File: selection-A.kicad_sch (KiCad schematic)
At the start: 4 parts, among them U0 74LS08, U10 74LS08, U12 74LS08, U13 74AHC1G32

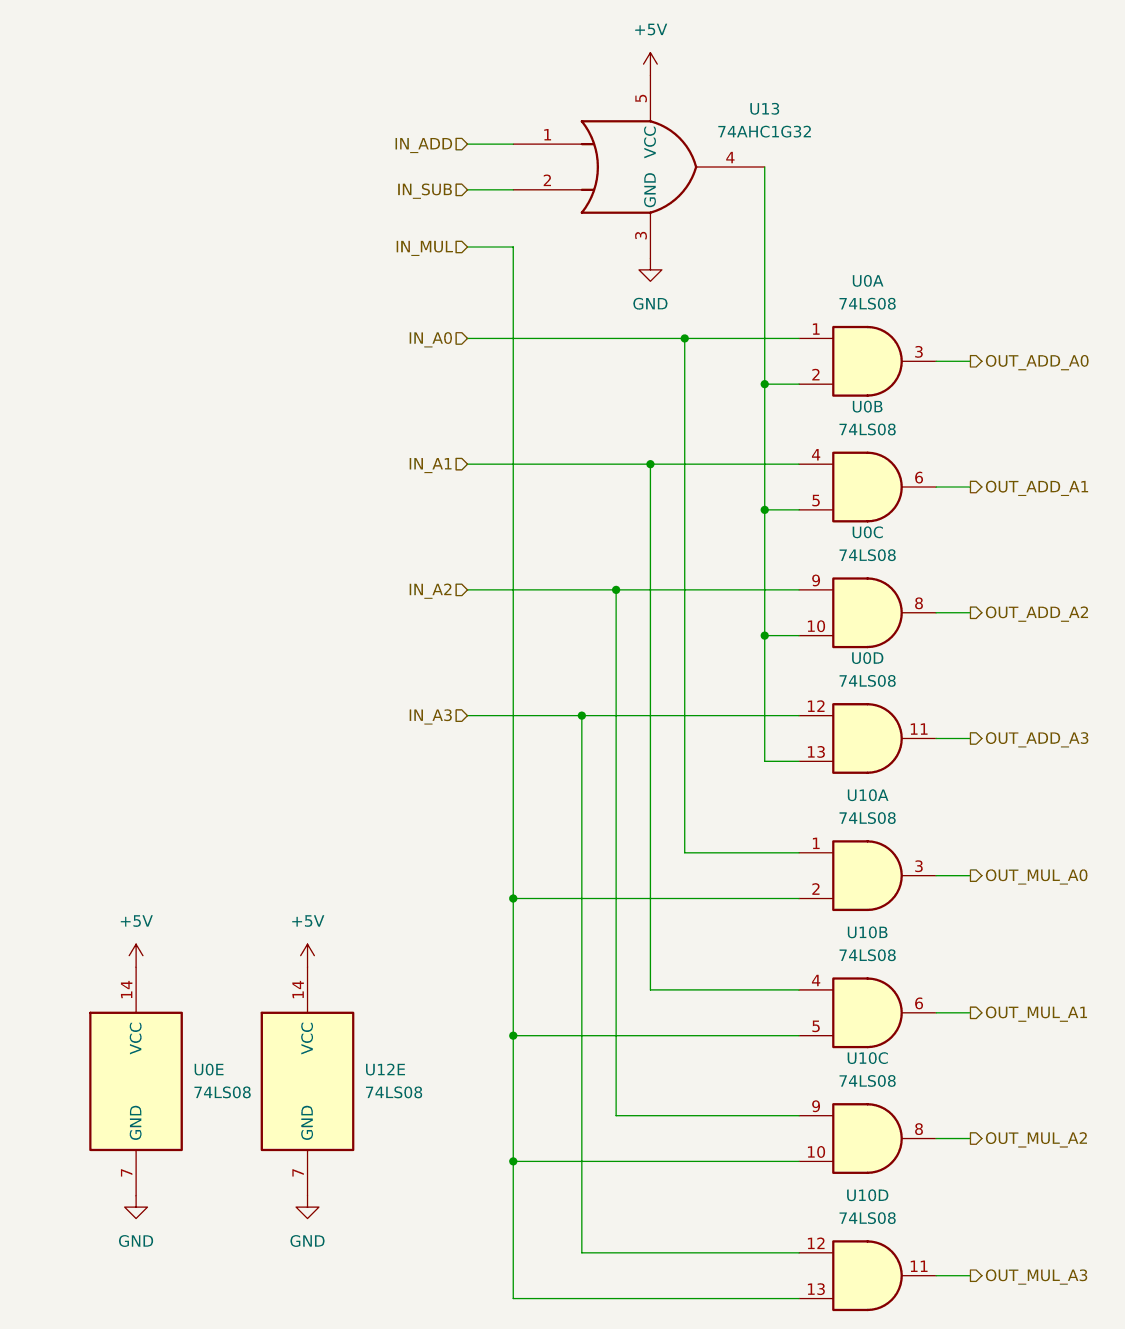
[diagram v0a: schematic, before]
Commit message: feat: removed ERC errors
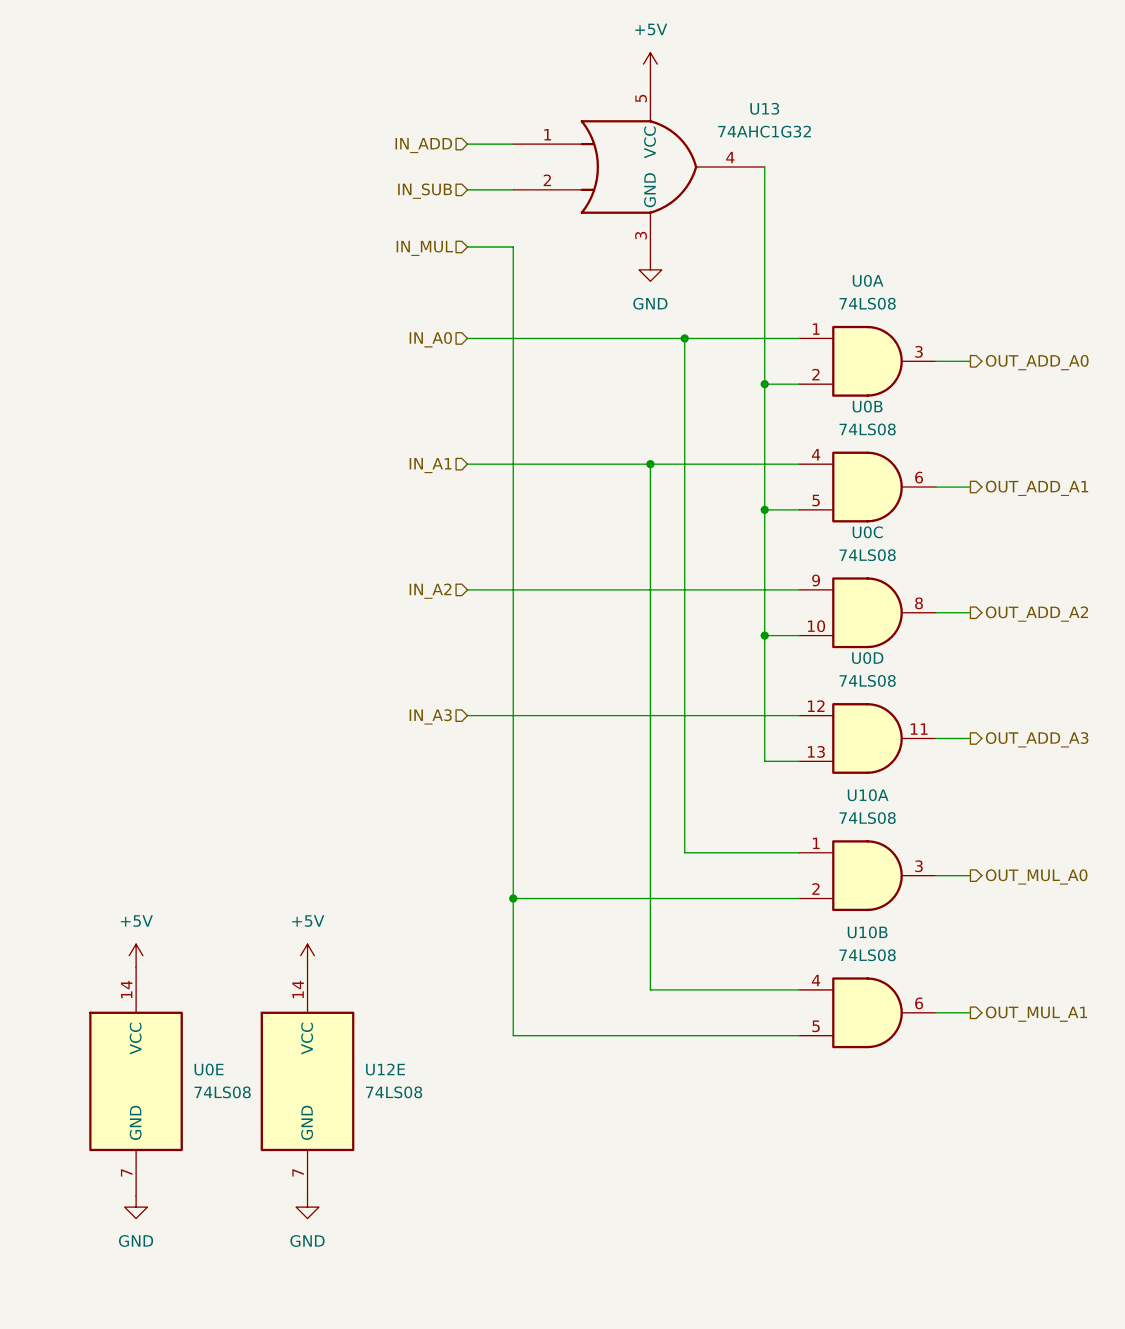
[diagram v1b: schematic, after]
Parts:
- removed unit 4 of U10
- removed unit 3 of U10

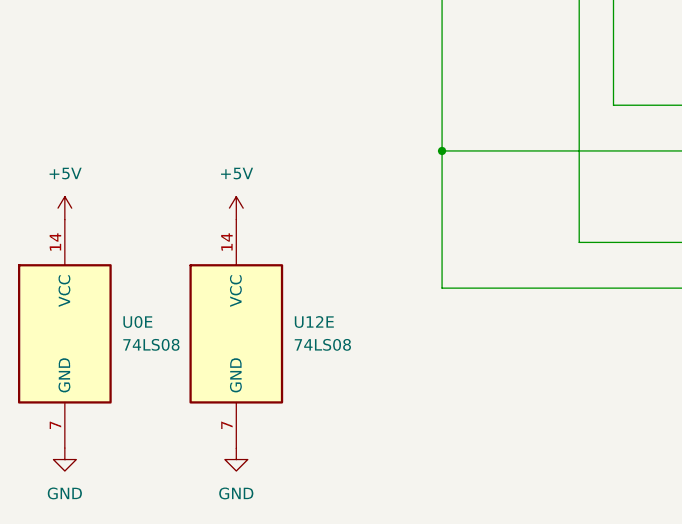
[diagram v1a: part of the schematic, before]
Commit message: fix: removed ERC warnings and errors
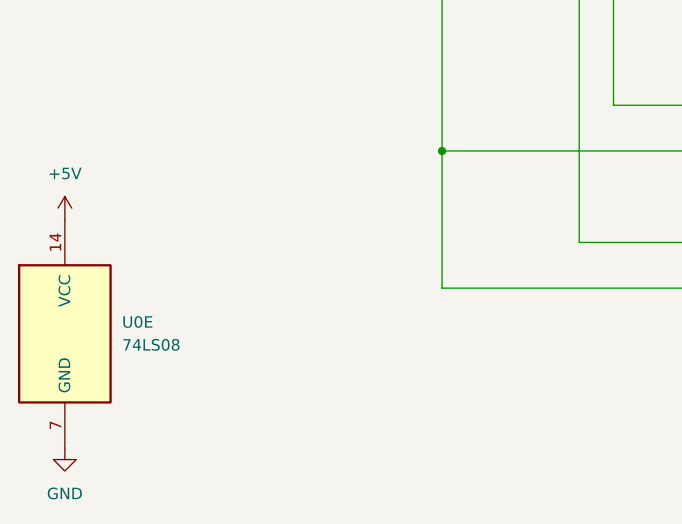
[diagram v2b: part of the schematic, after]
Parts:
- removed U12: 74LS08, symbol 74xx:74LS08
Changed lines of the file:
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@@
-	)
-	(symbol
-		(lib_id "power:GND")
-		(at 73.66 154.94 0)
-		(unit 1)
-		(exclude_from_sim no)
-		(in_bom yes)
-		(on_board yes)
-		(dnp no)
-		(fields_autoplaced yes)
-		(property "Reference" "#PWR025"
-			(at 73.66 161.29 0)
-			(effects
-				(font
-					(size 1.27 1.27)
-				)
-				(hide yes)
-			)
-		)
-		(property "Value" "GND"
-			(at 73.66 160.02 0)
-			(effects
-				(font
-					(size 1.27 1.27)
-				)
-			)
-		)
-		(property "Footprint" ""
-			(at 73.66 154.94 0)
-			(effects
-				(font
-					(size 1.27 1.27)
-				)
-				(hide yes)
-			)
-		)
-		(property "Datasheet" ""
-			(at 73.66 154.94 0)
-			(effects
-				(font
-					(size 1.27 1.27)
-				)
-				(hide yes)
-			)
-		)
-		(property "Description" "Power symbol creates a global label with name \"GND\" , ground"
-			(at 73.66 154.94 0)
-			(effects
-				(font
-					(size 1.27 1.27)
-				)
-				(hide yes)
-			)
-		)
-		(pin "1"
-		)
-		(instances
-			(project ""
-				(path "/4987240f-8890-46b8-b8e9-0d60580cb205/30c1ae8d-c878-40aa-ace0-371f489a4d3c"
-					(reference "#PWR025")
-					(unit 1)
-				)
-			)
-		)
 	)
 	(symbol
@@
 	(symbol
 		(lib_id "power:+5V")
-		(at 73.66 129.54 0)
-		(unit 1)
-		(exclude_from_sim no)
-		(in_bom yes)
-		(on_board yes)
-		(dnp no)
-		(fields_autoplaced yes)
-		(property "Reference" "#PWR06"
-			(at 73.66 133.35 0)
-			(effects
-				(font
-					(size 1.27 1.27)
-				)
-				(hide yes)
-			)
-		)
-		(property "Value" "+5V"
-			(at 73.66 124.46 0)
-			(effects
-				(font
-					(size 1.27 1.27)
-				)
-			)
-		)
-		(property "Footprint" ""
-			(at 73.66 129.54 0)
-			(effects
-				(font
-					(size 1.27 1.27)
-				)
-				(hide yes)
-			)
-		)
-		(property "Datasheet" ""
-			(at 73.66 129.54 0)
-			(effects
-				(font
-					(size 1.27 1.27)
-				)
-				(hide yes)
-			)
-		)
-		(property "Description" "Power symbol creates a global label with name \"+5V\""
-			(at 73.66 129.54 0)
-			(effects
-				(font
-					(size 1.27 1.27)
-				)
-				(hide yes)
-			)
-		)
-		(pin "1"
-		)
-		(instances
-			(project ""
-				(path "/4987240f-8890-46b8-b8e9-0d60580cb205/30c1ae8d-c878-40aa-ace0-371f489a4d3c"
-					(reference "#PWR06")
-					(unit 1)
-				)
-			)
-		)
-	)
-	(symbol
-		(lib_id "power:+5V")
 		(at 111.76 30.48 0)
 		(unit 1)
@@
 				)
 			)
-		)
-	)
-	(symbol
-		(lib_id "74xx:74LS08")
-		(at 73.66 142.24 0)
-		(unit 5)
-		(exclude_from_sim no)
-		(in_bom yes)
-		(on_board yes)
-		(dnp no)
-		(fields_autoplaced yes)
-		(property "Reference" "U12"
-			(at 80.01 140.9699 0)
-			(effects
-				(font
-					(size 1.27 1.27)
-				)
-				(justify left)
-			)
-		)
-		(property "Value" "74LS08"
-			(at 80.01 143.5099 0)
-			(effects
-				(font
-					(size 1.27 1.27)
-				)
-				(justify left)
-			)
-		)
-		(property "Footprint" ""
-			(at 73.66 142.24 0)
-			(effects
-				(font
-					(size 1.27 1.27)
-				)
-				(hide yes)
-			)
-		)
-		(property "Datasheet" "http://www.ti.com/lit/gpn/sn74LS08"
-			(at 73.66 142.24 0)
-			(effects
-				(font
-					(size 1.27 1.27)
-				)
-				(hide yes)
-			)
-		)
-		(property "Description" "Quad And2"
-			(at 73.66 142.24 0)
-			(effects
-				(font
-					(size 1.27 1.27)
-				)
-				(hide yes)
-			)
-		)
-		(pin "12"
-		)
-		(pin "14"
-		)
-		(pin "11"
-		)
-		(pin "7"
-		)
-		(pin "8"
-		)
-		(pin "10"
-		)
-		(pin "9"
-		)
-		(pin "6"
-		)
-		(pin "5"
-		)
-		(pin "4"
-		)
-		(pin "3"
-		)
-		(pin "2"
-		)
-		(pin "1"
-		)
-		(pin "13"
-		)
-		(instances
-			(project ""
-				(path "/4987240f-8890-46b8-b8e9-0d60580cb205/30c1ae8d-c878-40aa-ace0-371f489a4d3c"
-					(reference "U12")
-					(unit 5)
-				)
-			)

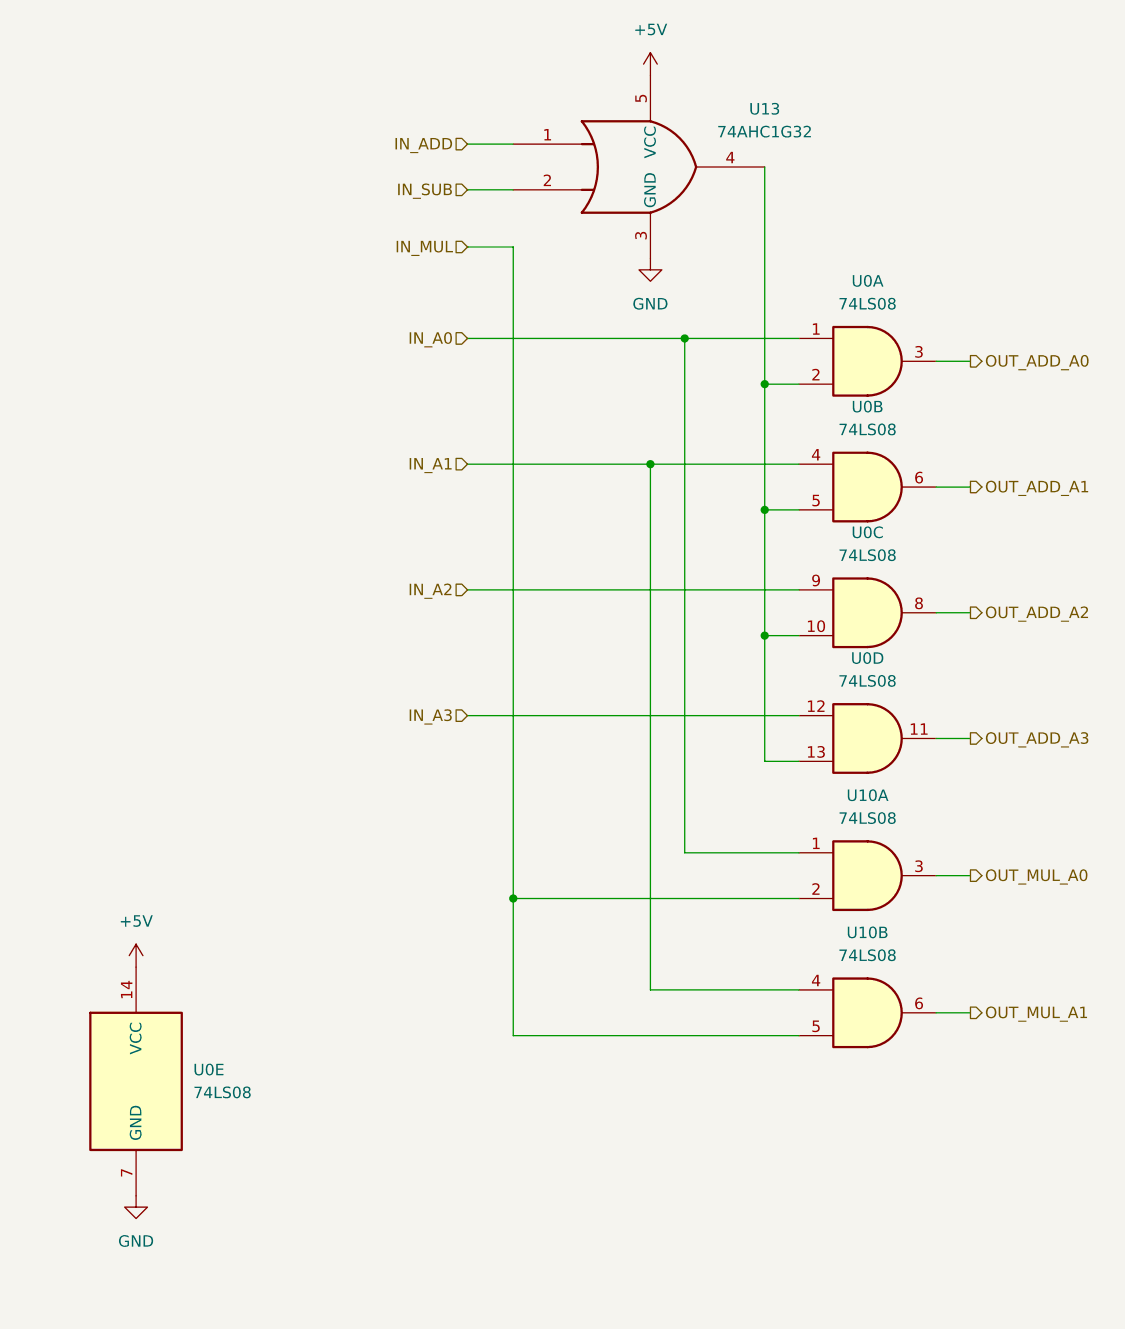
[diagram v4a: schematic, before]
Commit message: feat: footprints on gates
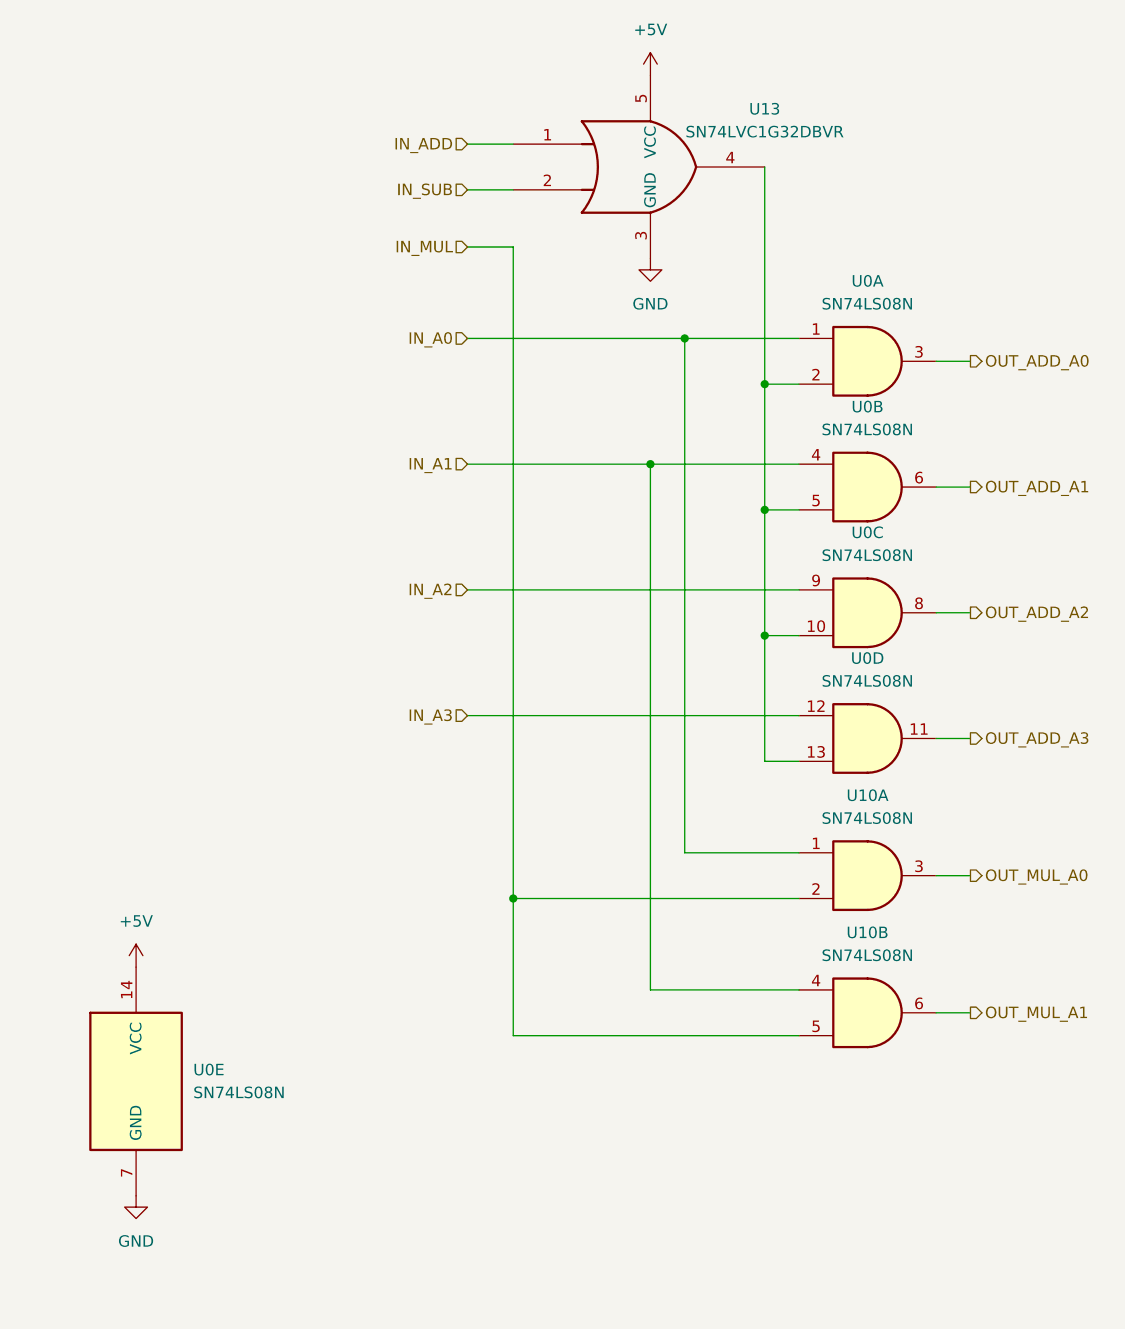
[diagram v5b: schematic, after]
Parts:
- U0, U10: value 74LS08 -> SN74LS08N; footprint (none) -> Package_DIP:DIP-14_W7.62mm_LongPads
- U13: value 74AHC1G32 -> SN74LVC1G32DBVR; footprint (none) -> Package_TO_SOT_SMD:SOT-23-5_HandSoldering
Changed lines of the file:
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@@
 			)
 		)
-		(property "Value" "74AHC1G32"
+		(property "Value" "SN74LVC1G32DBVR"
 			(at 124.46 36.7598 0)
 			(show_name no)
@@
 			)
 		)
-		(property "Footprint" ""
+		(property "Footprint" "Package_TO_SOT_SMD:SOT-23-5_HandSoldering"
 			(at 111.76 40.64 0)
 			(hide yes)
@@
 			)
 		)
-		(property "Value" "74LS08"
+		(property "Value" "SN74LS08N"
 			(at 135.8817 69.85 0)
 			(show_name no)
@@
 			)
 		)
-		(property "Footprint" ""
+		(property "Footprint" "Package_DIP:DIP-14_W7.62mm_LongPads"
 			(at 135.89 76.2 0)
 			(hide yes)
@@
 			)
 		)
-		(property "Datasheet" "http://www.ti.com/lit/gpn/sn74LS08"
+		(property "Datasheet" "https://www.ti.com/lit/ds/symlink/sn74hc86.pdf"
 			(at 135.89 76.2 0)
 			(hide yes)
@@
 			)
 		)
-		(property "Value" "74LS08"
+		(property "Value" "SN74LS08N"
 			(at 135.8817 113.03 0)
 			(show_name no)
@@
 			)
 		)
-		(property "Footprint" ""
+		(property "Footprint" "Package_DIP:DIP-14_W7.62mm_LongPads"
 			(at 135.89 119.38 0)
 			(hide yes)
@@
 			)
 		)
-		(property "Datasheet" "http://www.ti.com/lit/gpn/sn74LS08"
+		(property "Datasheet" "https://www.ti.com/lit/ds/symlink/sn74hc86.pdf"
 			(at 135.89 119.38 0)
 			(hide yes)
@@
 			)
 		)
-		(property "Value" "74LS08"
+		(property "Value" "SN74LS08N"
 			(at 135.8817 128.27 0)
 			(show_name no)
@@
 			)
 		)
-		(property "Footprint" ""
+		(property "Footprint" "Package_DIP:DIP-14_W7.62mm_LongPads"
 			(at 135.89 134.62 0)
 			(hide yes)
@@
 			)
 		)
-		(property "Datasheet" "http://www.ti.com/lit/gpn/sn74LS08"
+		(property "Datasheet" "https://www.ti.com/lit/ds/symlink/sn74hc86.pdf"
 			(at 135.89 134.62 0)
 			(hide yes)
@@
 			)
 		)
-		(property "Value" "74LS08"
+		(property "Value" "SN74LS08N"
 			(at 135.8817 97.79 0)
 			(show_name no)
@@
 			)
 		)
-		(property "Footprint" ""
+		(property "Footprint" "Package_DIP:DIP-14_W7.62mm_LongPads"
 			(at 135.89 104.14 0)
 			(hide yes)
@@
 			)
 		)
-		(property "Datasheet" "http://www.ti.com/lit/gpn/sn74LS08"
+		(property "Datasheet" "https://www.ti.com/lit/ds/symlink/sn74hc86.pdf"
 			(at 135.89 104.14 0)
 			(hide yes)
@@
 			)
 		)
-		(property "Value" "74LS08"
+		(property "Value" "SN74LS08N"
 			(at 60.96 143.5099 0)
 			(show_name no)
@@
 			)
 		)
-		(property "Footprint" ""
+		(property "Footprint" "Package_DIP:DIP-14_W7.62mm_LongPads"
 			(at 54.61 142.24 0)
 			(hide yes)
@@
 			)
 		)
-		(property "Datasheet" "http://www.ti.com/lit/gpn/sn74LS08"
+		(property "Datasheet" "https://www.ti.com/lit/ds/symlink/sn74hc86.pdf"
 			(at 54.61 142.24 0)
 			(hide yes)
@@
 			)
 		)
-		(property "Value" "74LS08"
+		(property "Value" "SN74LS08N"
 			(at 135.8817 55.88 0)
 			(show_name no)
@@
 			)
 		)
-		(property "Footprint" ""
+		(property "Footprint" "Package_DIP:DIP-14_W7.62mm_LongPads"
 			(at 135.89 62.23 0)
 			(hide yes)
@@
 			)
 		)
-		(property "Datasheet" "http://www.ti.com/lit/gpn/sn74LS08"
+		(property "Datasheet" "https://www.ti.com/lit/ds/symlink/sn74hc86.pdf"
 			(at 135.89 62.23 0)
 			(hide yes)
@@
 			)
 		)
-		(property "Value" "74LS08"
+		(property "Value" "SN74LS08N"
 			(at 135.8817 83.82 0)
 			(show_name no)
@@
 			)
 		)
-		(property "Footprint" ""
+		(property "Footprint" "Package_DIP:DIP-14_W7.62mm_LongPads"
 			(at 135.89 90.17 0)
 			(hide yes)
@@
 			)
 		)
-		(property "Datasheet" "http://www.ti.com/lit/gpn/sn74LS08"
+		(property "Datasheet" "https://www.ti.com/lit/ds/symlink/sn74hc86.pdf"
 			(at 135.89 90.17 0)
 			(hide yes)
